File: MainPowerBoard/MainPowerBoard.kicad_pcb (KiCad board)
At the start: 2 copper layers, 177.8 x 177.8 mm, 259 parts, among them J101 CONN_01X04, J102 CONN_01X04, J103 CONN_01X04, J104 CONN_01X02, J105 CONN_01X02, J106 CONN_01X06, J107 CONN_01X06, J108 CONN_01X04, J109 CONN_01X04, J110 CONN_01X02, J111 CONN_01X02, J112 CONN_01X02, J113 CONN_01X02, J114 CONN_01X02, J115 CONN_01X02, J116 CONN_01X02, J117 CONN_01X02, J118 CONN_01X02, J119 CONN_01X02, J120 CONN_01X02, J121 CONN_01X02, J122 CONN_01X02, J123 CONN_01X02, J124 CONN_01X02, J125 CONN_01X02, J126 CONN_01X02, J127 CONN_01X02, J128 CONN_01X02, J129 CONN_01X02, J130 MOUNTING_HOLE, J131 MOUNTING_HOLE, J132 MOUNTING_HOLE, J133 MOUNTING_HOLE, Q1 CSD19502Q5B, Q2 CSD19502Q5B, SW701 KS-01Q-01, U1 LTC4357MPMS8, U1001 LMR16030S, U1101 LMR16030S, U1201 LMR16030S, U1301 LMR16030S, U1401 LMR16030S, U2 LTC4357MPMS8, U201 LMR16030S, U301 LMR16030S, U701 AP2204RA-5.0TRG1, U702 TLV271IDBVR, U703 LTC2950-1, U704 TLC393, U801 LMR16030S, U901 LMR16030S

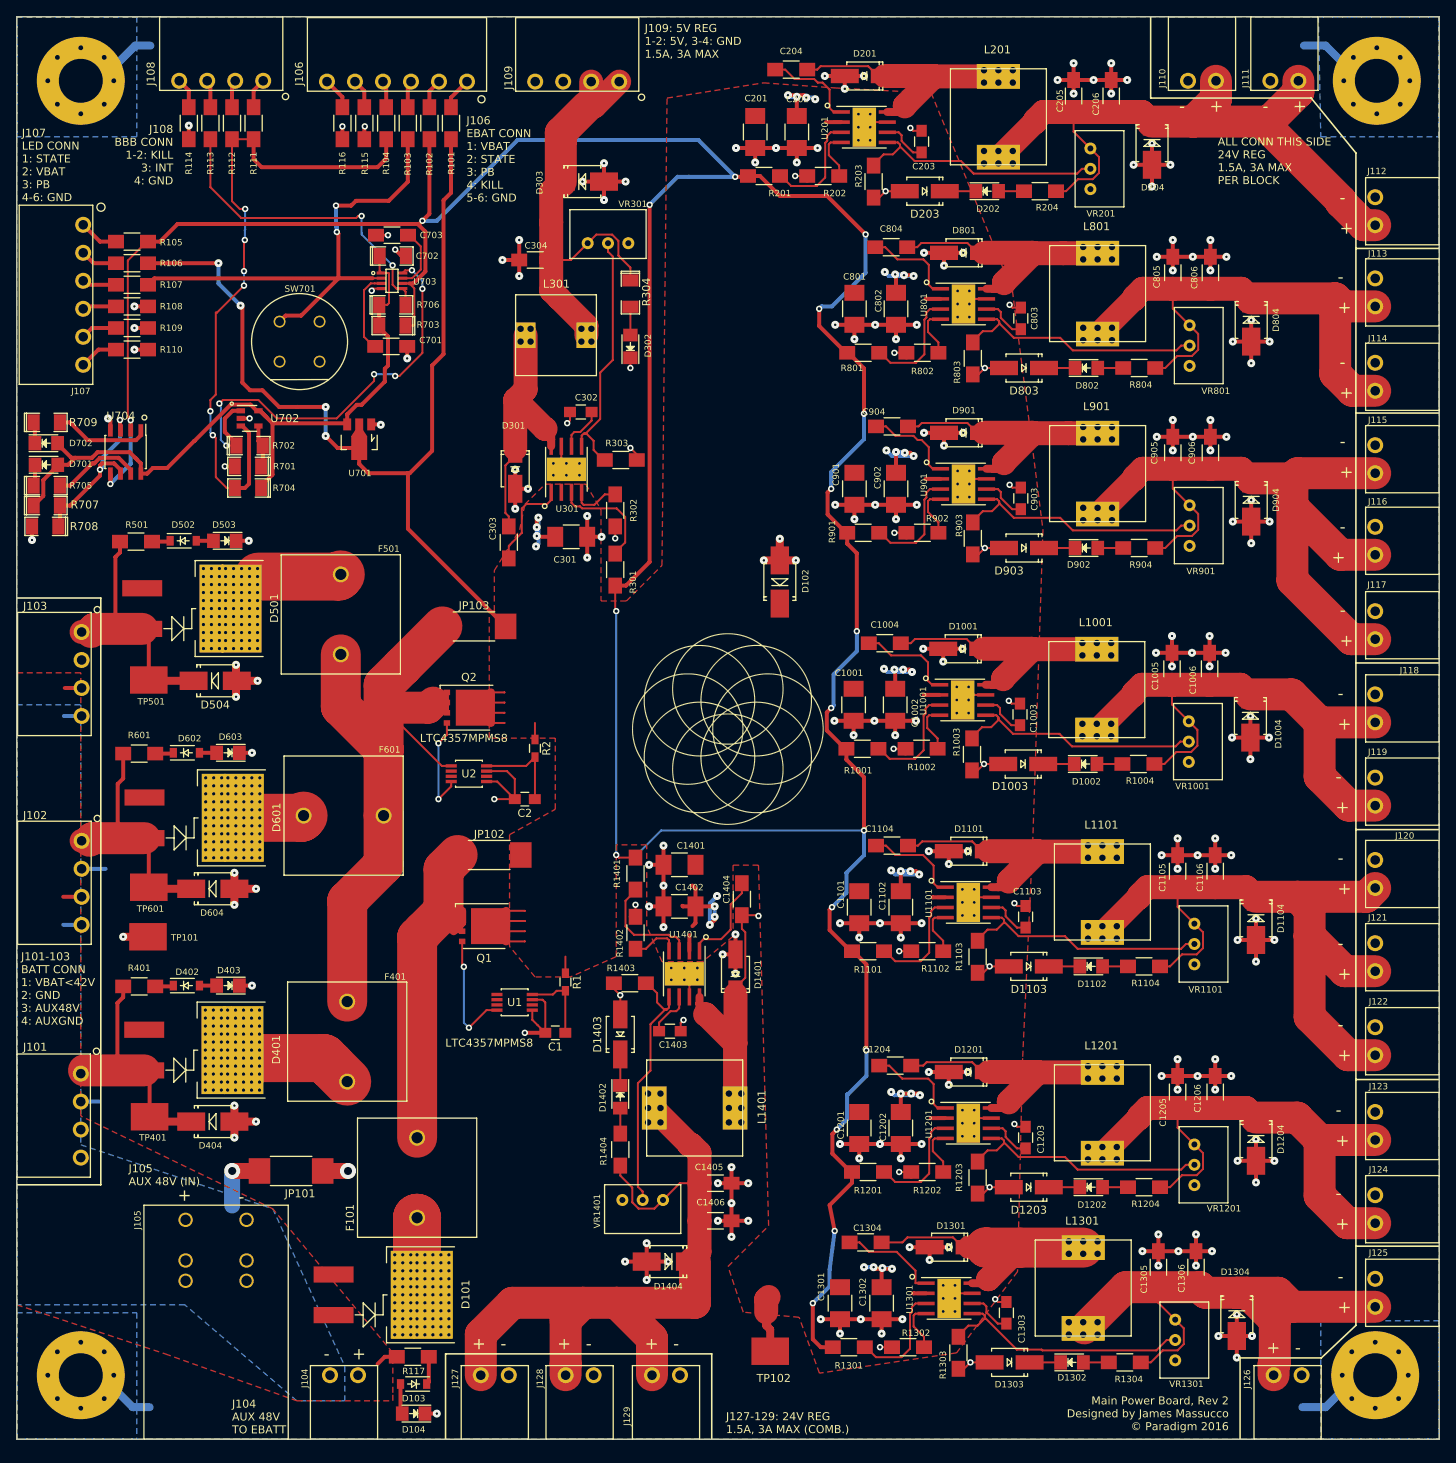
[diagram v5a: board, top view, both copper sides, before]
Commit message: Finalized Power Selector Circuit
Replaced Schottky Diodes with Ideal Diodes. Converted 8th 24V Rail to
second 5V rail.
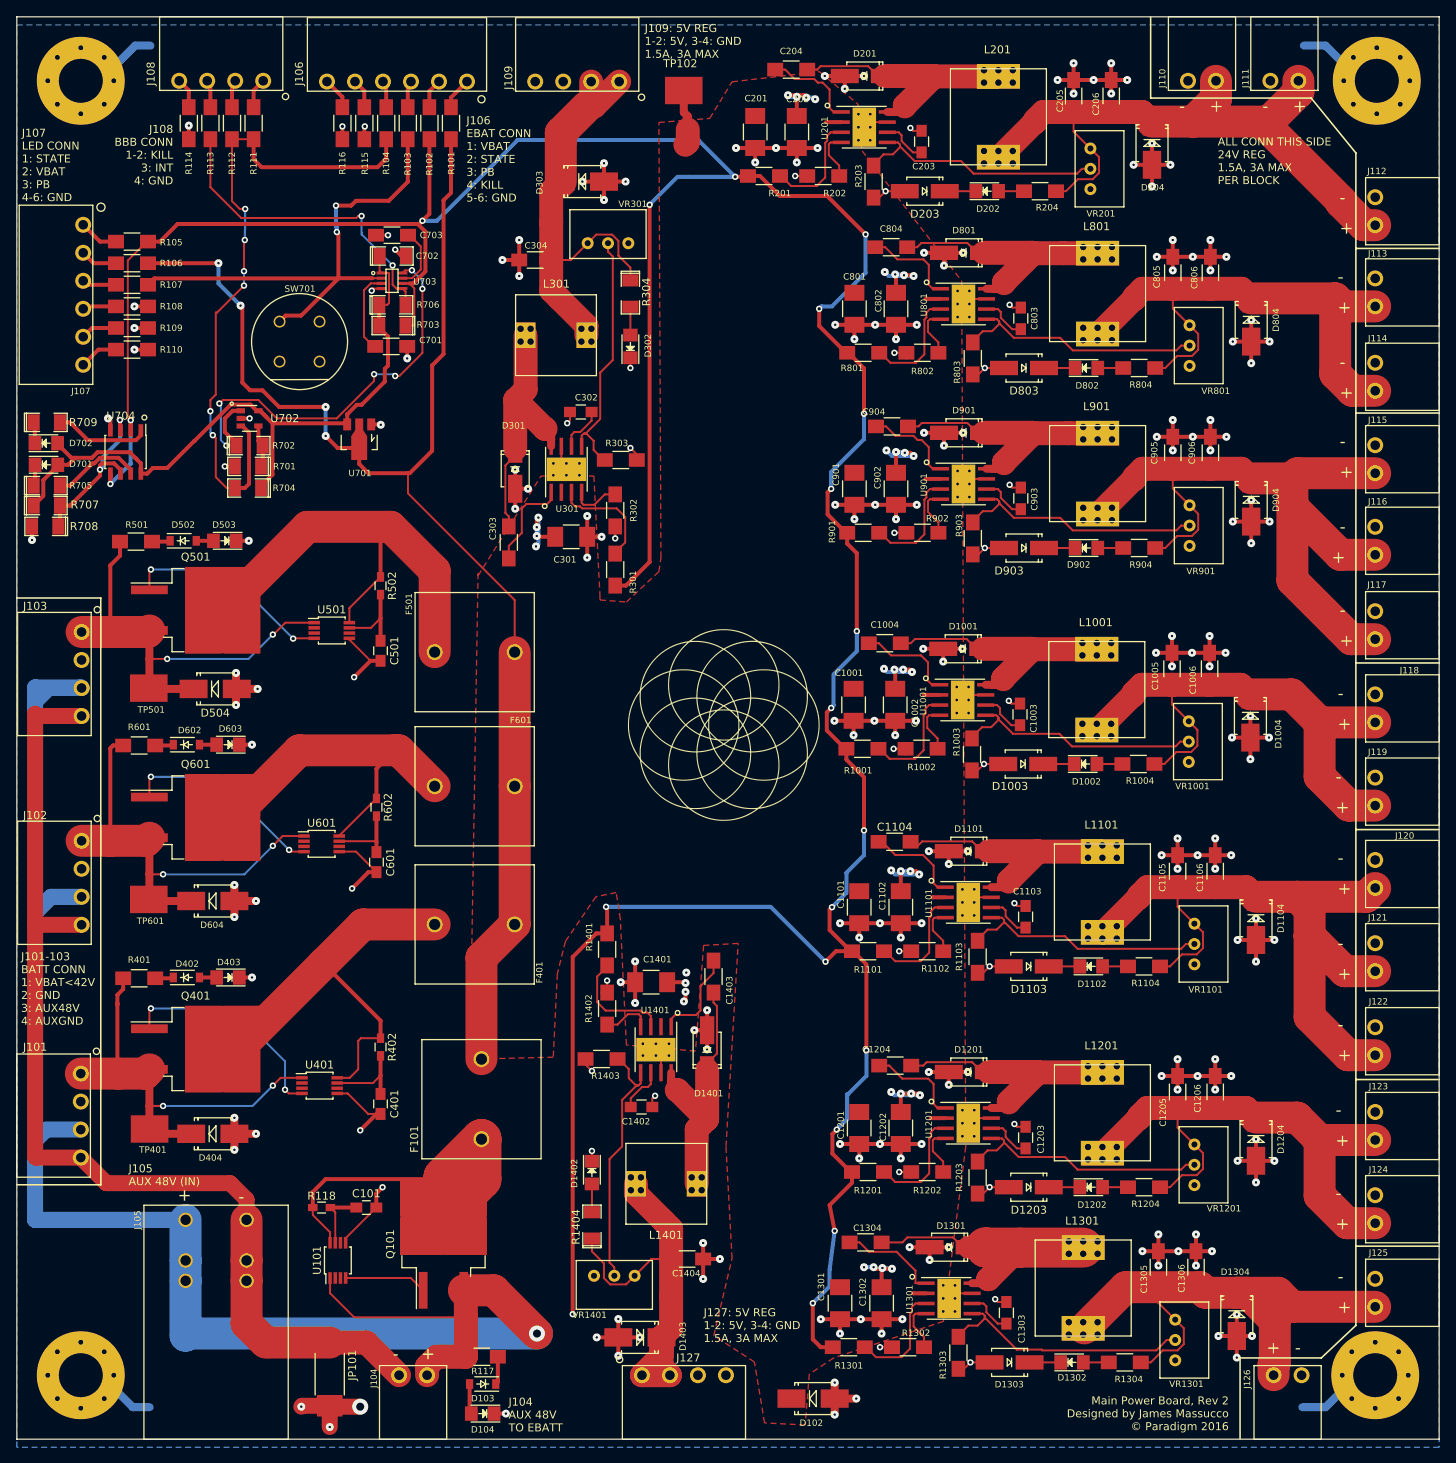
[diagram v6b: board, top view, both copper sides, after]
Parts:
- removed C1, C2: 1u, Capacitors_SMD:C_0805_HandSoldering
- removed C1405, C1406: 4.7uF, Capacitors_SMD:C_1206_HandSoldering
- removed D101, D401, D501, D601: VB30100S-E3/8W, hyperCustom:DD-PAK_TO263_SingleDiode_ThermalVias
- removed D1404: 28V, Diodes_SMD:SMB_Handsoldering
- removed J128, J129: CONN_01X02, hyperCustom:CONN_PHOENIX_1844210_2PIN
- removed JP102, JP103: JUMPER, Resistors_SMD:R_2512_HandSoldering
- removed Q1, Q2: CSD19502Q5B, TO_SOT_Packages_SMD:TDSON-8-1
- removed R1, R2: 100, Resistors_SMD:R_0603_HandSoldering
- removed TP101: Testpoint, hyperCustom:TP_SMT_Keystone
- removed U1, U2: LTC4357MPMS8, hyperCustom:LTC4357MPMS8
- added C101: 1u, Capacitors_SMD:C_0805_HandSoldering, F.Cu at (43.7, 148.8)
- added C401: 1u, Capacitors_SMD:C_0805_HandSoldering, F.Cu at (45.5, 135.9)
- added C501: 1u, Capacitors_SMD:C_0805_HandSoldering, F.Cu at (45.5, 79.2)
- added C601: 1u, Capacitors_SMD:C_0805_HandSoldering, F.Cu at (45.0, 105.7)
- added Q101: FDB3632, TO_SOT_Packages_SMD:TO-263-2, F.Cu at (53.3, 153.4)
- added Q401: FDB3632, TO_SOT_Packages_SMD:TO-263-2, F.Cu at (22.4, 129.0)
- added Q501: FDB3632, TO_SOT_Packages_SMD:TO-263-2, F.Cu at (22.4, 74.2)
- added Q601: FDB3632, TO_SOT_Packages_SMD:TO-263-2, F.Cu at (22.4, 100.1)
- added R118: 100, Resistors_SMD:R_0603_HandSoldering, F.Cu at (38.1, 148.8)
- added R402: 100, Resistors_SMD:R_0603_HandSoldering, F.Cu at (45.5, 128.8)
- added R502: 100, Resistors_SMD:R_0603_HandSoldering, F.Cu at (45.5, 71.1)
- added R602: 100, Resistors_SMD:R_0603_HandSoldering, F.Cu at (45.0, 98.8)
- added U101: LTC4357MPMS8, Housings_SSOP:MSOP-8_3x3mm_Pitch0.65mm, F.Cu at (40.1, 155.4)
- added U401: LTC4357MPMS8, Housings_SSOP:MSOP-8_3x3mm_Pitch0.65mm, F.Cu at (37.8, 133.6)
- added U501: LTC4357MPMS8, Housings_SSOP:MSOP-8_3x3mm_Pitch0.65mm, F.Cu at (39.4, 76.7)
- added U601: LTC4357MPMS8, Housings_SSOP:MSOP-8_3x3mm_Pitch0.65mm, F.Cu at (38.1, 103.4)
- C1402: footprint Capacitors_SMD:C_1210_HandSoldering -> Resistors_SMD:R_0805_HandSoldering
- C1403: value 2.2uF -> 0.1uF; footprint Resistors_SMD:R_0805_HandSoldering -> Resistors_SMD:R_1206_HandSoldering
- C1404: value 0.1uF -> 47uF; footprint Resistors_SMD:R_1206_HandSoldering -> Capacitors_SMD:C_1206_HandSoldering
- D1403: value 18V -> 7.5V; footprint Diodes_SMD:SMA_Handsoldering -> Diodes_SMD:SMB_Handsoldering
- J106: footprint CONN_PHOENIX_1844252_6PIN -> hyperCustom:CONN_PHOENIX_1844252_6PIN
- J127: value CONN_01X02 -> CONN_01X04; footprint hyperCustom:CONN_PHOENIX_1844210_2PIN -> hyperCustom:CONN_PHOENIX_1844236_4PIN_1
- L1401: value 47uH -> 15uH; footprint hyperCustom:47uIND_CDRH127_LDNP-470MC_SUMIDA_heatsink -> hyperCustom:15uIND_SLF10165T-150M3R13PF_BOURNS_heatsink
- R1403: value 20k -> 12k
- R1404: value 400 -> 300; footprint Resistors_SMD:R_1206_HandSoldering -> SMD_Packages:SMD-1206_Pol
- VR1401: value 1M -> 100k
- moved TP102 158.0 mm to (83.4, 9.22), turned to 180 degrees
- moved D102 102.2 mm to (99.5, 172.7), turned to 0 degrees
- moved C1404 45.5 mm to (83.8, 155.3), turned to 0 degrees
- moved D1403 38.0 mm to (77.9, 165.1), turned to 180 degrees
- moved JP101 25.9 mm to (39.1, 169.7), turned to 90 degrees
- moved F501 25.8 mm to (49.8, 86.9), turned to 0 degrees
- moved C1402 25.5 mm to (78.1, 136.3), turned to 0 degrees
- moved J127 20.1 mm to (75.7, 177.8)
- moved F601 16.8 mm to (49.8, 103.6)
- moved C1401 15.1 mm to (79.3, 120.7)
- moved F401 14.7 mm to (49.8, 120.9), turned to 0 degrees
- moved F101 12.7 mm to (65.5, 142.7)
- moved R1404 10.1 mm to (71.9, 151.1)
- moved R1403 10.1 mm to (73.1, 130.3)
- moved U1401 10.1 mm to (79.9, 129.1)
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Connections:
- C1402 pad 1: /MAIN_POWER -> Net-(C1402-Pad1)
- C1403 pad 2: GND -> Net-(C1403-Pad2)
- C1404 pad 1: Net-(C1404-Pad1) -> /5V0_REG2
- C1404 pad 2: Net-(C1404-Pad2) -> GND
- D1401 pad 1: Net-(C1404-Pad2) -> Net-(C1403-Pad2)
- D1402 pad 1: Net-(D1402-Pad1) -> GND
- D1403 pad 1: Net-(D1402-Pad1) -> /5V0_REG2
- F101 pad 2: /48V0_FROM_LINE -> /MAIN_POWER
- F401 pad 2: /VCC_BATT_COMB -> /MAIN_POWER
- F501 pad 2: /VCC_BATT_COMB -> /MAIN_POWER
- F601 pad 2: /VCC_BATT_COMB -> /MAIN_POWER
- J127 pad 2: GND -> /5V0_REG2
- JP101 pad 1: /GND_FROM_LINE -> GND
- JP101 pad 2: GND -> /GND_FROM_LINE
- L1401 pad 1: Net-(C1404-Pad2) -> Net-(C1403-Pad2)
- L1401 pad 2: /5 Volt Regulator -- 2/24V0_REG -> /5V0_REG2
- R1404 pad 1: /5 Volt Regulator -- 2/24V0_REG -> /5V0_REG2
- U1401 pad 1: Net-(C1404-Pad1) -> Net-(C1403-Pad1)
- U1401 pad 6: Net-(C1403-Pad1) -> Net-(C1402-Pad1)
- U1401 pad 8: Net-(C1404-Pad2) -> Net-(C1403-Pad2)
- VR1401 pad 3: /5 Volt Regulator -- 2/24V0_REG -> /5V0_REG2
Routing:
- net /48V0_FROM_LINE_UNPROT: track 7.17 -> 218.7 mm, vias 0 -> 4
- net /GND_FROM_LINE: track 12.2 -> 133.1 mm, vias 1 -> 0
- net /VCC_BATT_COMB: track 87.7 -> 0.00 mm
- net Net-(F101-Pad1): track 5.64 -> 54.4 mm
- net Net-(F501-Pad1): track 10.4 -> 59.1 mm
- net /48V0_FROM_LINE: track 47.9 -> 0.00 mm
- net Net-(C1404-Pad2): track 47.4 -> 0.00 mm, vias 1 -> 0
- net /5 Volt Regulator -- 2/24V0_REG: track 44.2 -> 0.00 mm
- net Net-(F601-Pad1): track 6.22 -> 45.4 mm
- net Net-(C1403-Pad2): track 0.00 -> 32.9 mm
- net Net-(Q401-Pad1): track 0.00 -> 28.0 mm, vias 0 -> 2
- net Net-(Q501-Pad1): track 0.00 -> 26.6 mm, vias 0 -> 2
- net Net-(Q601-Pad1): track 0.00 -> 25.6 mm, vias 0 -> 2
- net /VCC_BATT1: track 32.7 -> 58.2 mm, vias 0 -> 2
- net /VCC_BATT2: track 32.8 -> 58.2 mm, vias 0 -> 2
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- removed copper zone on F.Cu, net /48V0_FROM_LINE_UNPROT
- removed copper zone on B.Cu, net /GND_FROM_LINE
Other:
- net class VBATT removed
- board text added: "J127: 5V REG 1-2: 5V, 3-4: GND 1.5A, 3A MAX"
- board text removed: "J127-129: 24V REG 1.5A, 3A MAX (COMB.)"

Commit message: Small Misc Changes
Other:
- board text added: "Main Power Board, Rev 3 Designed by James Massucco Updated by Darryl Day © Paradigm 2017"
- board text removed: "Main Power Board, Rev 2 Designed by James Massucco © Paradigm 2016"
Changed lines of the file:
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@@
     (links 628)
     (no_connects 41)
-    (area -0.075001 -0.075001 177.875001 177.875001)
+    (area -5.675 -5.675 182.885 183.575)
     (thickness 1.6)
     (drawings 74)
@@
   (layers
     (0 F.Cu signal)
-    (31 B.Cu signal)
+    (31 B.Cu signal hide)
     (32 B.Adhes user)
     (33 F.Adhes user)
@@
   )
   (setup
-    (last_trace_width 1)
+    (last_trace_width 0.25)
     (user_trace_width 0.5)
     (user_trace_width 1)
@@
   (module hyperCustom:TP_SMT_Keystone (layer F.Cu)
     (at 83.371 9.217 180)
-    (fp_text reference TP102 (at 0.44 3.375 180) (layer F.SilkS)
+    (fp_text reference TP102 (at 0.567 2.613 180) (layer F.SilkS)
       (effects (font (size 1 1) (thickness 0.15)))
     )
@@
     (effects (font (size 1 1) (thickness 0.15)) (justify left))
   )
-  (gr_text "Main Power Board, Rev 2\nDesigned by James Massucco\n© Paradigm 2016" (at 151.5 174.6) (layer F.SilkS)
-    (effects (font (size 1 1) (thickness 0.15)) (justify right))
+  (gr_text "Main Power Board, Rev 3\nDesigned by James Massucco\nUpdated by Darryl Day\n© Paradigm 2017" (at 151.5 174.6) (layer F.SilkS)
+    (effects (font (size 0.7 0.7) (thickness 0.15)) (justify right))
   )
   (gr_text - (at 27.7 147.5) (layer F.SilkS)
